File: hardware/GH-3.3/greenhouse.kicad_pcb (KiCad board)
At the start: 2 copper layers, 170 x 100 mm, 154 parts, among them K1 OMRON G5LE, K2 OMRON G5LE, K3 OMRON G5LE, K4 OMRON G5LE, K5 OMRON G5LE, K6 OMRON G5LE, K7 OMRON G5LE, U1 PC847, X1 PH PROBE, X10 ANALOG INPUT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

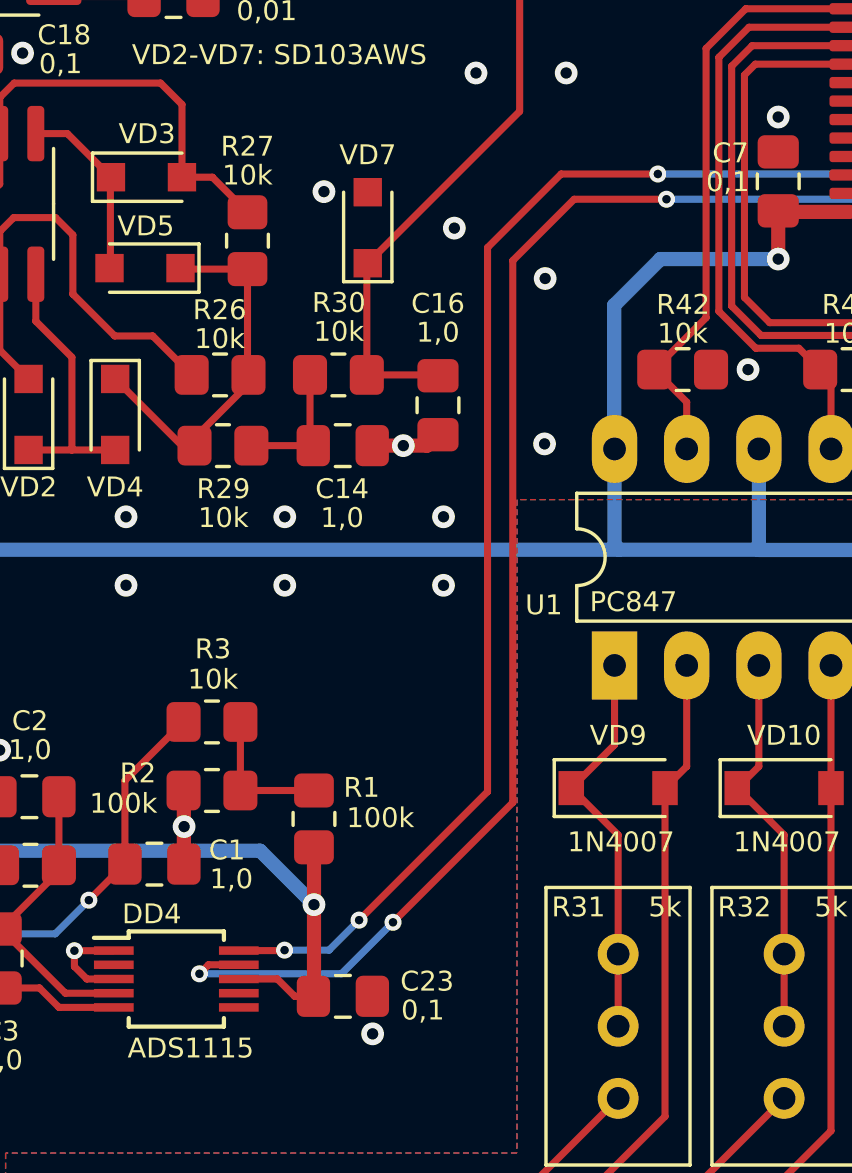
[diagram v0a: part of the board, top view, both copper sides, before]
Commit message: fix: update hw to kicad 7, fix capacitor placement in 4.0dev
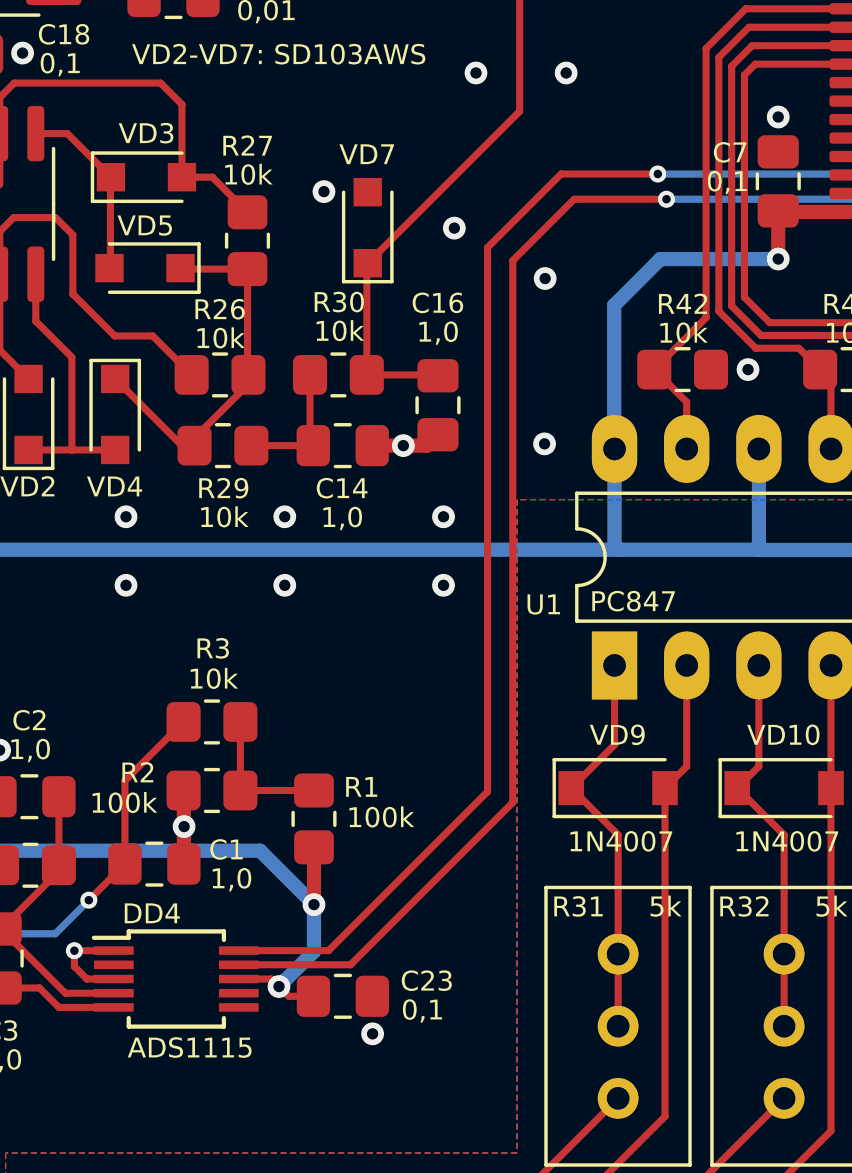
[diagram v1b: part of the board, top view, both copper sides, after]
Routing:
- net I2C_SDA0: track 125.3 -> 122.3 mm, vias 7 -> 5
- net +3V3: track 464.9 -> 465.1 mm, vias 88 -> 89
- net I2C_SCL0: vias 5 -> 3
